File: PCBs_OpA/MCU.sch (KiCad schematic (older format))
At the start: 21 parts, among them CON2 AVR-ISP-6, J10 SPK, U6 ATMEGA328P-AU, Y2 20Mhz

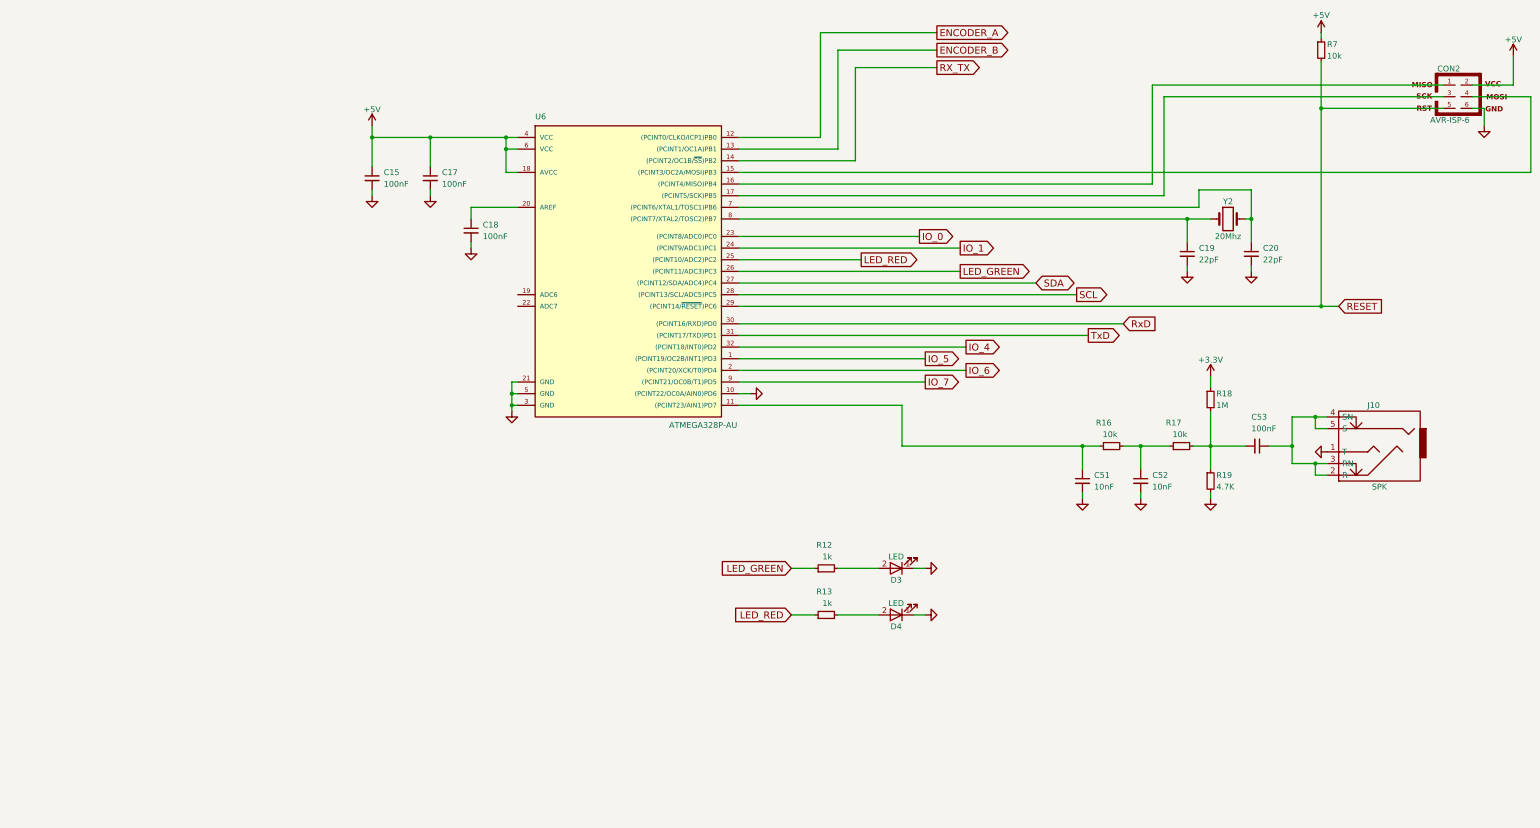
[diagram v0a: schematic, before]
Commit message: add LPF/HPF RFSimm models
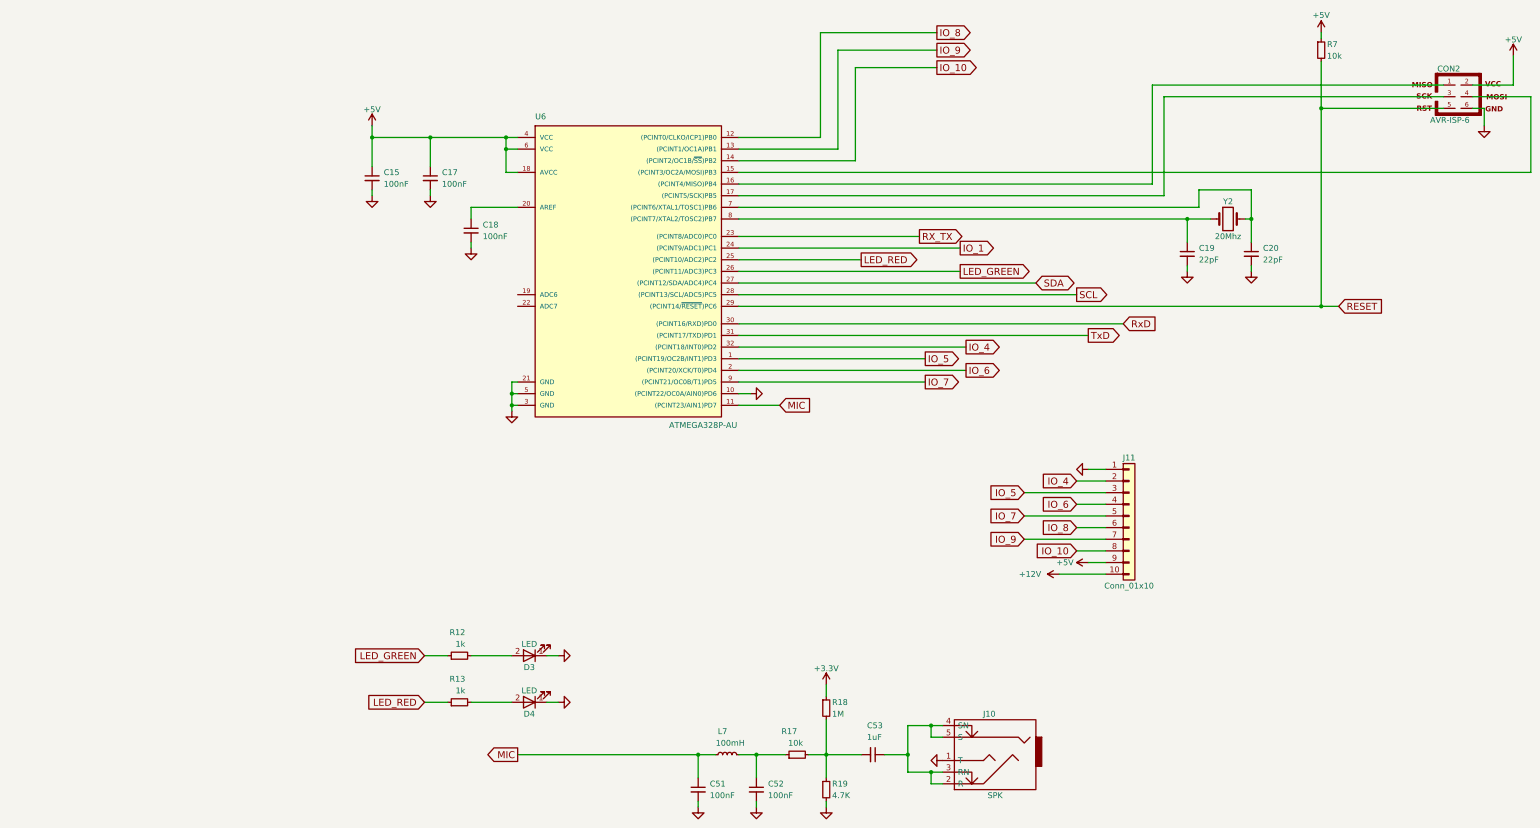
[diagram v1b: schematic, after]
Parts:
- removed R16: 10k, LCSDR:R_1206_0603, symbol R_Small
- added J11: Conn_01x10, Pin_Headers:Pin_Header_Straight_1x10_Pitch2.54mm, symbol Conn_01x10
- added L7: 100mH, Choke_Toroid_ThroughHole:Choke_Toroid_8x16mm_Vertical, symbol L_Small
- C51, C52: value 10nF -> 100nF
- C53: value 100nF -> 1uF
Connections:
- net IO_0 is gone; now on net RX_TX: U6.23 ((PCINT8/ADC0)PC0)
- net +5V: now also J11.9 (Pin_9)
- net GND: now also J11.1 (Pin_1)
- net IO_4: now also J11.2 (Pin_2)
- net IO_5: now also J11.3 (Pin_3)
- net IO_6: now also J11.4 (Pin_4)
- net IO_7: now also J11.5 (Pin_5)
- net RX_TX: no longer U6.14 ((PCINT2/OC1B/~SS~)PB2)
- net MIC: now reaches C51.1, U6.11 ((PCINT23/AIN1)PD7)
- net MIC: now also L7.1
- net at C52.1, R17.1: now also L7.2
- net ENCODER_A renamed IO_8
- net IO_8: now also J11.6 (Pin_6)
- net ENCODER_B renamed IO_9
- net IO_9: now also J11.7 (Pin_7)
- new net +12V: J11.10 (Pin_10)
- new net IO_10: J11.8 (Pin_8), U6.14 ((PCINT2/OC1B/~SS~)PB2)
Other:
- moved on the sheet: C51, C52, C53, D3, D4, J10, R12, R13, R17, R18, R19

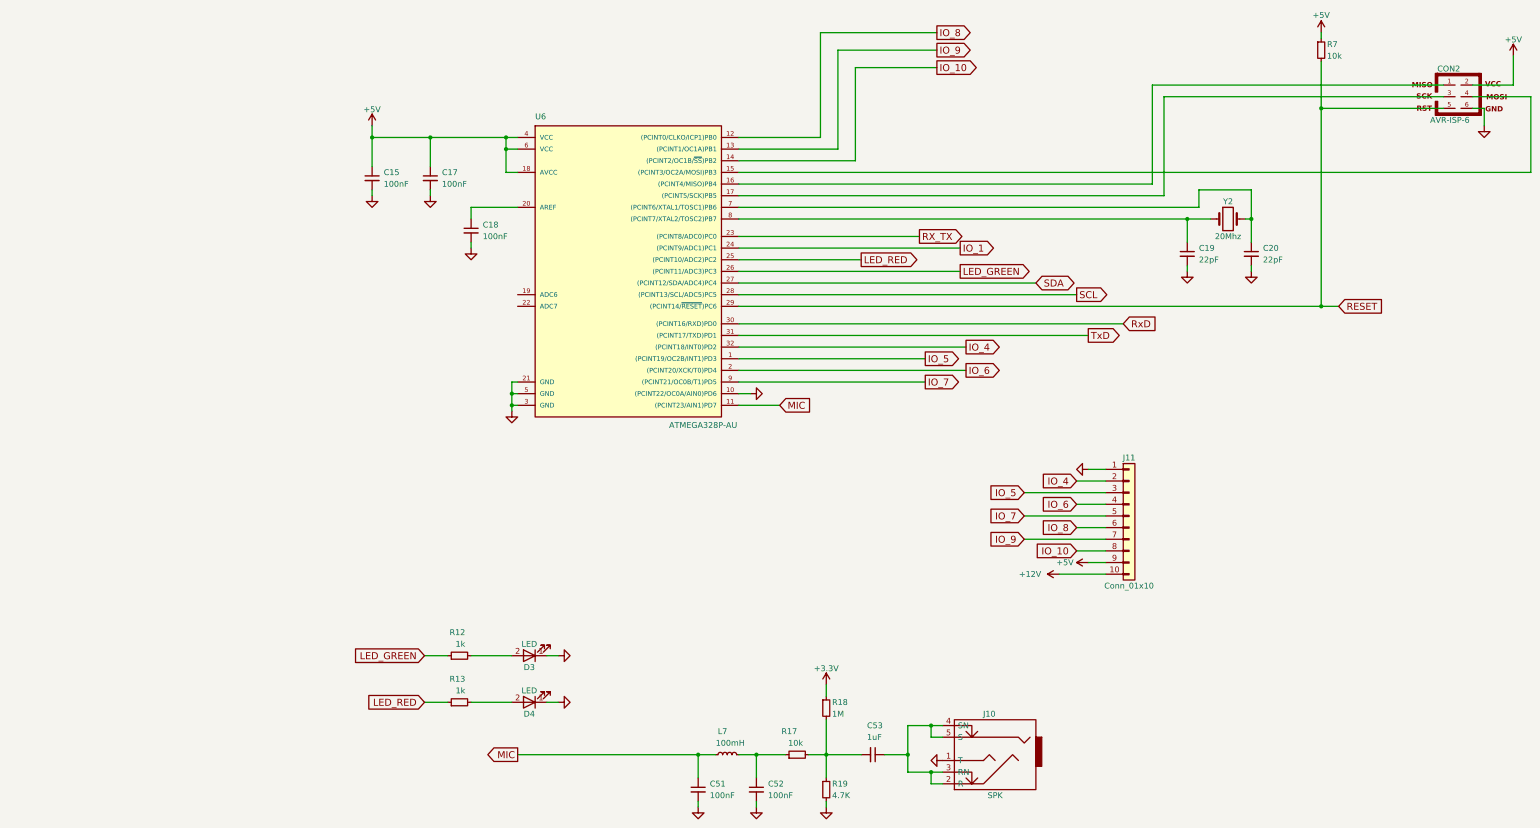
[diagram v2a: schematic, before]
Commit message: Arduino Nano PCB ADX988 DSP
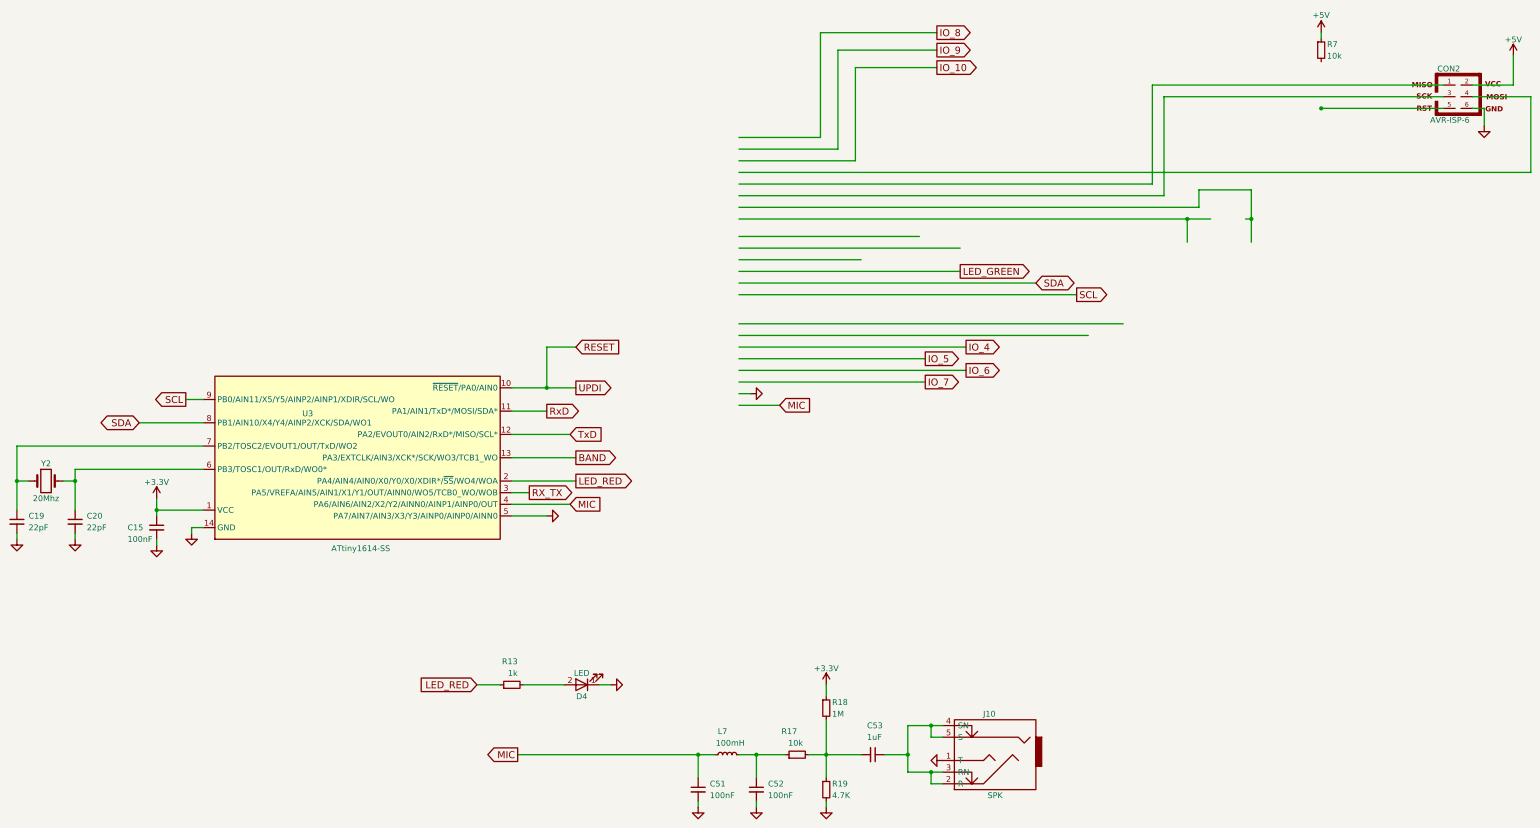
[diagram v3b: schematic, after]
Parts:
- removed C17, C18: 100nF, LCSDR:C_1206_0603, symbol C_Small
- removed D3: LED, LEDs:LED_D3.0mm_Horizontal_O3.81mm_Z10.0mm, symbol LED
- removed J11: Conn_01x10, Pin_Headers:Pin_Header_Straight_1x10_Pitch2.54mm, symbol Conn_01x10
- removed R12: 1k, LCSDR:R_1206_0603, symbol R_Small
- removed U6: ATMEGA328P-AU, Housings_QFP:TQFP-32_7x7mm_Pitch0.8mm, symbol ATMEGA328P-AU
- added U3: ATtiny1614-SS, Housings_SOIC:SOIC-14_3.9x8.7mm_Pitch1.27mm, symbol ATtiny1614-SS
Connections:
- net labels added: BAND, UPDI
- net labels removed: +12V, IO_1
- wire segments 98 -> 91
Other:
- moved on the sheet: C19, C20, D4, R13, Y2

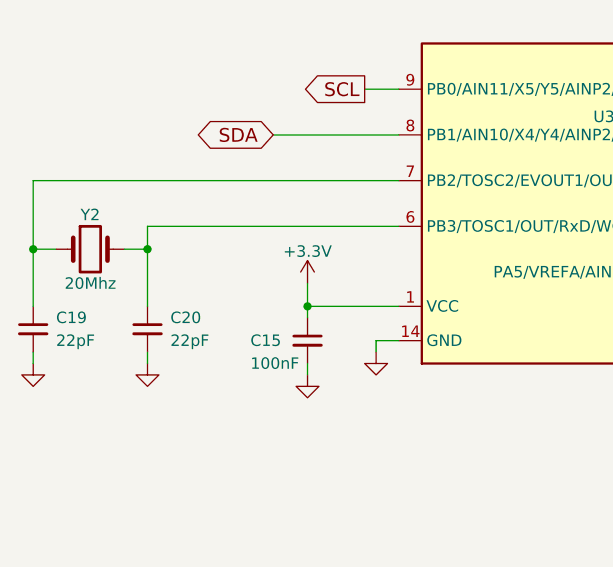
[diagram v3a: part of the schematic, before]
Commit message: Migrate to LGT8F328p
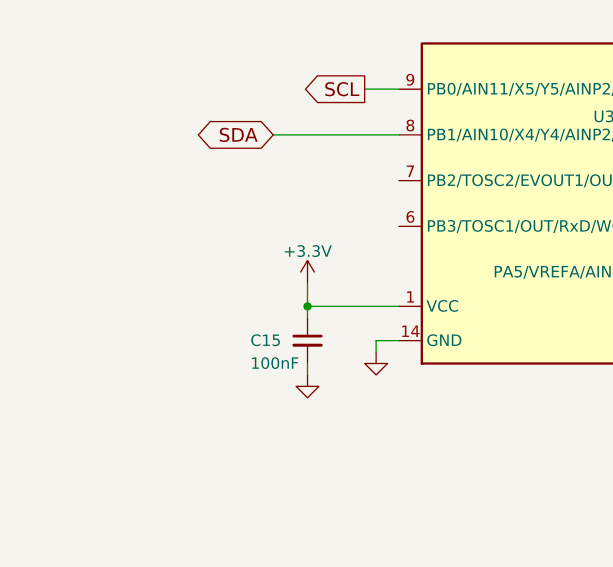
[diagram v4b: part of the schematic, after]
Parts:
- removed C19, C20: 22pF, LCSDR:C_1206_0603, symbol C_Small
- removed Y2: 20Mhz, Crystals:Crystal_HC49-U_Vertical, symbol Crystal
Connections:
- wire segments 91 -> 83
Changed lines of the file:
@@
 Comment4 ""
 $EndDescr
-$Comp
-L Crystal Y2
-U 1 1 6253E0F5
-P -1800 4600
-F 0 "Y2" H -1800 4750 50  0000 C CNN
-F 1 "20Mhz" H -1800 4450 50  0000 C CNN
-F 2 "Crystals:Crystal_HC49-U_Vertical" H -1800 4600 50  0001 C CNN
-F 3 "" H -1800 4600 50  0001 C CNN
-	1    -1800 4600
-	1    0    0    -1
-$EndComp
-$Comp
-L C_Small C19
-U 1 1 6253E0FC
-P -2050 4950
-F 0 "C19" H -1950 5000 50  0000 L CNN
-F 1 "22pF" H -1950 4900 50  0000 L CNN
-F 2 "LCSDR:C_1206_0603" H -2050 4950 50  0001 C CNN
-F 3 "" H -2050 4950 50  0001 C CNN
-	1    -2050 4950
-	1    0    0    -1
-$EndComp
-$Comp
-L C_Small C20
-U 1 1 6253E103
-P -1550 4950
-F 0 "C20" H -1450 5000 50  0000 L CNN
-F 1 "22pF" H -1450 4900 50  0000 L CNN
-F 2 "LCSDR:C_1206_0603" H -1550 4950 50  0001 C CNN
-F 3 "" H -1550 4950 50  0001 C CNN
-	1    -1550 4950
-	1    0    0    -1
-$EndComp
-$Comp
-L GND #PWR027
-U 1 1 6253E10A
-P -2050 5100
-F 0 "#PWR027" H -2050 4850 50  0001 C CNN
-F 1 "GND" H -2050 4950 50  0001 C CNN
-F 2 "" H -2050 5100 50  0001 C CNN
-F 3 "" H -2050 5100 50  0001 C CNN
-	1    -2050 5100
-	1    0    0    -1
-$EndComp
-$Comp
-L GND #PWR028
-U 1 1 6253E110
-P -1550 5100
-F 0 "#PWR028" H -1550 4850 50  0001 C CNN
-F 1 "GND" H -1550 4950 50  0001 C CNN
-F 2 "" H -1550 5100 50  0001 C CNN
-F 3 "" H -1550 5100 50  0001 C CNN
-	1    -1550 5100
-	1    0    0    -1
-$EndComp
 Text GLabel 6700 2900 2    60   BiDi ~ 0
 SDA
@@
 Connection ~ 8000 2350
 Connection ~ 8550 2350
-Wire Wire Line
-	-2050 5100 -2050 5050
-Wire Wire Line
-	-1550 5100 -1550 5050
 Wire Wire Line
 	4150 2900 6700 2900
@@
 	1    0    0    -1
 $EndComp
-Wire Wire Line
-	-2050 4300 -450 4300
 Text GLabel 2700 4800 2    60   Input ~ 0
 MIC
@@
 	2200 4000 2500 4000
 Wire Wire Line
-	-1650 4600 -1550 4600
-Connection ~ -1550 4600
-Wire Wire Line
-	-2050 4300 -2050 4850
-Wire Wire Line
 	-850 4750 -850 4900
 $Comp
@@
 	-850 4850 -450 4850
 Wire Wire Line
-	-1550 4500 -1550 4850
-Wire Wire Line
-	-1550 4500 -450 4500
-Wire Wire Line
-	-1950 4600 -2050 4600
-Connection ~ -2050 4600
-Wire Wire Line
 	2200 4200 2700 4200
